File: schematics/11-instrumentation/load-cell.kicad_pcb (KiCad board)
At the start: 4 copper layers, 17.8 x 17.1 mm, 14 parts, among them IC1 HX711, Q1 S8550

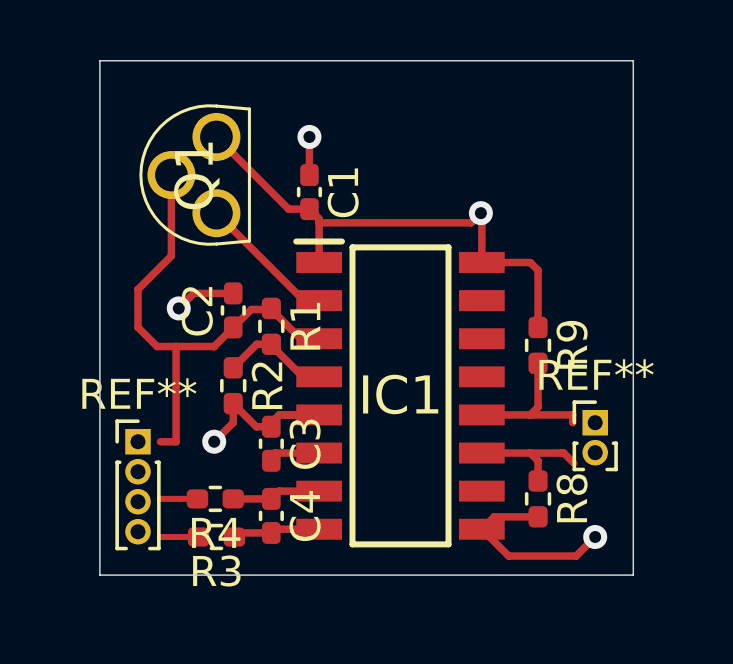
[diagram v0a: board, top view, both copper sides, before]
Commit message: load cell pcb edited
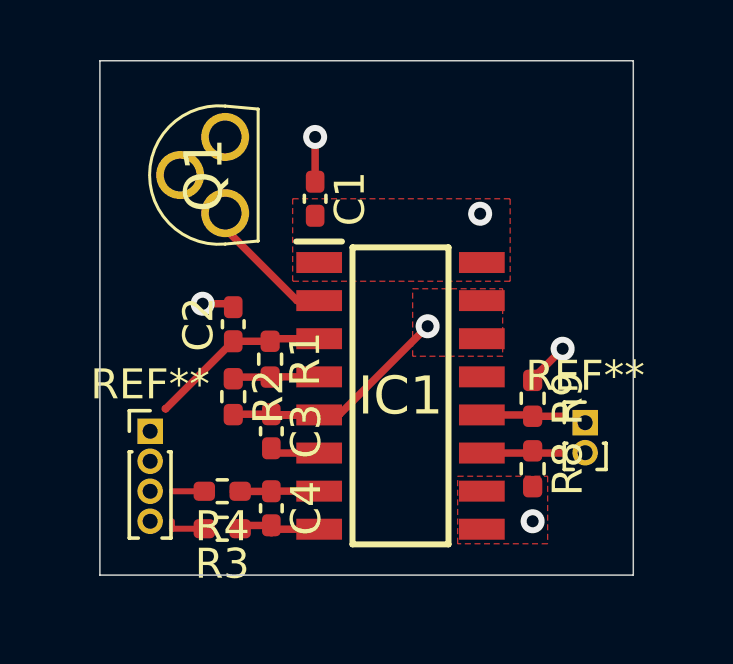
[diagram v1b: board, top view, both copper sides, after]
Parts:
- moved R9 1.77 mm to (145.9, 95.8)
- moved R1 1.10 mm to (137.1, 94.5)
- moved R8 1.02 mm to (145.9, 98.2)
- moved REF** 0.54 mm to (133.1, 96.9)
- moved C2 0.46 mm to (135.9, 93.3)
- moved C3 0.42 mm to (137.2, 96.9)
- moved R2 0.37 mm to (135.9, 95.8)
- moved R4 0.34 mm to (135.5, 98.9)
- moved R3 0.34 mm to (135.5, 100.2)
- moved REF** 0.34 mm to (147.6, 96.6)
- moved C1 0.29 mm to (138.6, 89.2)
- moved Q1 0.29 mm to (135.6, 89.6)
- moved C4 0.25 mm to (137.2, 99.5)
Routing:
- net 1v8: track 33.5 -> 7.59 mm, vias 1 -> 2
- net GND: track 15.8 -> 10.9 mm
- net /DT: track 5.12 -> 2.61 mm
- net /SCK: track 4.24 -> 2.73 mm
- net Net-(IC1-Pad4): track 3.62 -> 2.91 mm
- added copper zone on F.Cu, net 1v8
- added copper zone on F.Cu, net GND
